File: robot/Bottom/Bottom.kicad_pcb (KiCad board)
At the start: 2 copper layers, 40 x 40 mm, 39 parts, among them M1 Stepper_Motor_bipolar, M2 Stepper_Motor_bipolar, U1 GP2S60, U2 GP2S60, U7 DRV8833PWP, U8 DRV8833PWP

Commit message: Changes to structure
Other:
- outline, holes or cut-outs redrawn
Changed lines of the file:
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@@
-(kicad_pcb (version 20171130) (host pcbnew "(5.1.2)-1")
+(kicad_pcb (version 20171130) (host pcbnew "(5.1.4)-1")
   (general
     (thickness 1.6)
-    (drawings 21)
+    (drawings 23)
     (tracks 283)
     (zones 0)
@@
   )
   (setup
-    (last_trace_width 0.3)
+    (last_trace_width 0.2)
     (user_trace_width 0.2)
     (user_trace_width 0.25)
@@
     )
   )
+  (gr_line (start 159 93) (end 159 110.8) (layer Edge.Cuts) (width 0.1))
+  (gr_line (start 153 110.8) (end 159 110.8) (layer Edge.Cuts) (width 0.1))
+  (gr_line (start 153 113) (end 153 110.8) (layer Edge.Cuts) (width 0.1))
+  (gr_line (start 193 110.8) (end 187 110.8) (layer Edge.Cuts) (width 0.1))
+  (gr_line (start 187 93) (end 187 110.8) (layer Edge.Cuts) (width 0.1))
+  (gr_line (start 193 113) (end 193 110.8) (layer Edge.Cuts) (width 0.1))
   (gr_line (start 187 93) (end 193 93) (layer Edge.Cuts) (width 0.1))
   (gr_line (start 159 93) (end 153 93) (layer Edge.Cuts) (width 0.1))
-  (gr_line (start 159 113) (end 159 93) (layer Edge.Cuts) (width 0.1))
-  (gr_line (start 153 113) (end 159 113) (layer Edge.Cuts) (width 0.1))
-  (gr_line (start 187 113) (end 187 93) (layer Edge.Cuts) (width 0.1))
-  (gr_line (start 193 113) (end 187 113) (layer Edge.Cuts) (width 0.1))
   (gr_line (start 153 93) (end 153 78) (layer Edge.Cuts) (width 0.1))
   (gr_line (start 153 118) (end 153 113) (layer Edge.Cuts) (width 0.1))

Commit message: Small changes, connectors
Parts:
- added H20: GND, Custom:Mounting_Pad_Power, F.Cu at (154.2, 115.5)
- added H21: GND, Custom:Mounting_Pad_Power, F.Cu at (191.8, 115.5)
- added J1: Conn_01x02, Custom:BG300-02-A-L-A, F.Cu at (173.0, 102.6)
- C10, C11, C12, C13, C8, C9: footprint Capacitors_SMD:C_0805 -> Capacitor_SMD:C_0805_2012Metric
- R1, R11, R12, R13, R14, R2, R3, R4: footprint Resistors_SMD:R_0805 -> Resistor_SMD:R_0805_2012Metric
- moved M1 1.50 mm to (164.7, 112.8)
- moved M2 1.50 mm to (181.3, 112.8)
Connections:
- U7 pad 8: (no net) -> Net-(U7-Pad8)
- U8 pad 8: (no net) -> Net-(U8-Pad8)
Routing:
- net Net-(M2-Pad1): track 23.7 -> 25.7 mm
- net Net-(M2-Pad3): track 14.4 -> 12.9 mm
- net Net-(M1-Pad3): track 15.7 -> 17.2 mm
- net Net-(M1-Pad1): track 16.3 -> 14.8 mm
- net Net-(M2-Pad2): track 15.8 -> 14.4 mm
- net Net-(M2-Pad4): track 13.3 -> 12.3 mm
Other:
- outline, holes or cut-outs redrawn

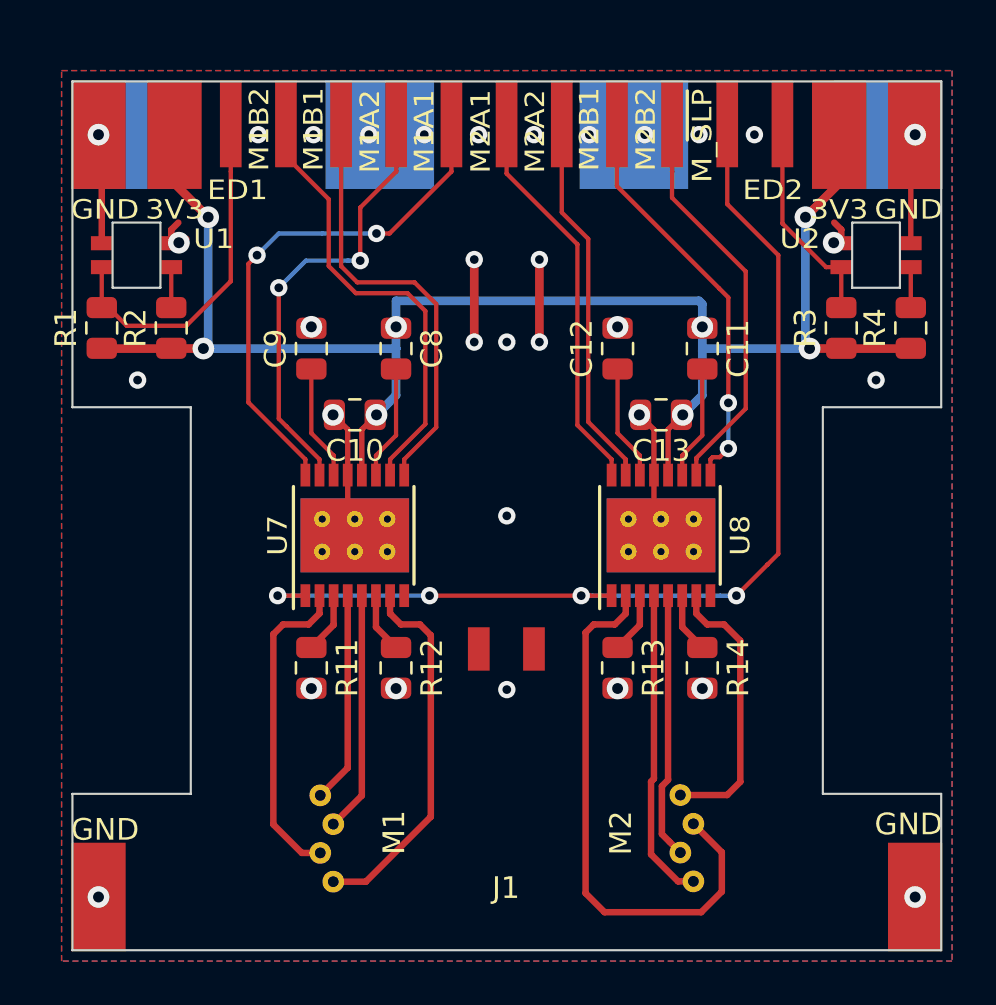
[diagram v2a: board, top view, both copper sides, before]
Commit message: Add VBS, Add Silk deco, small changes
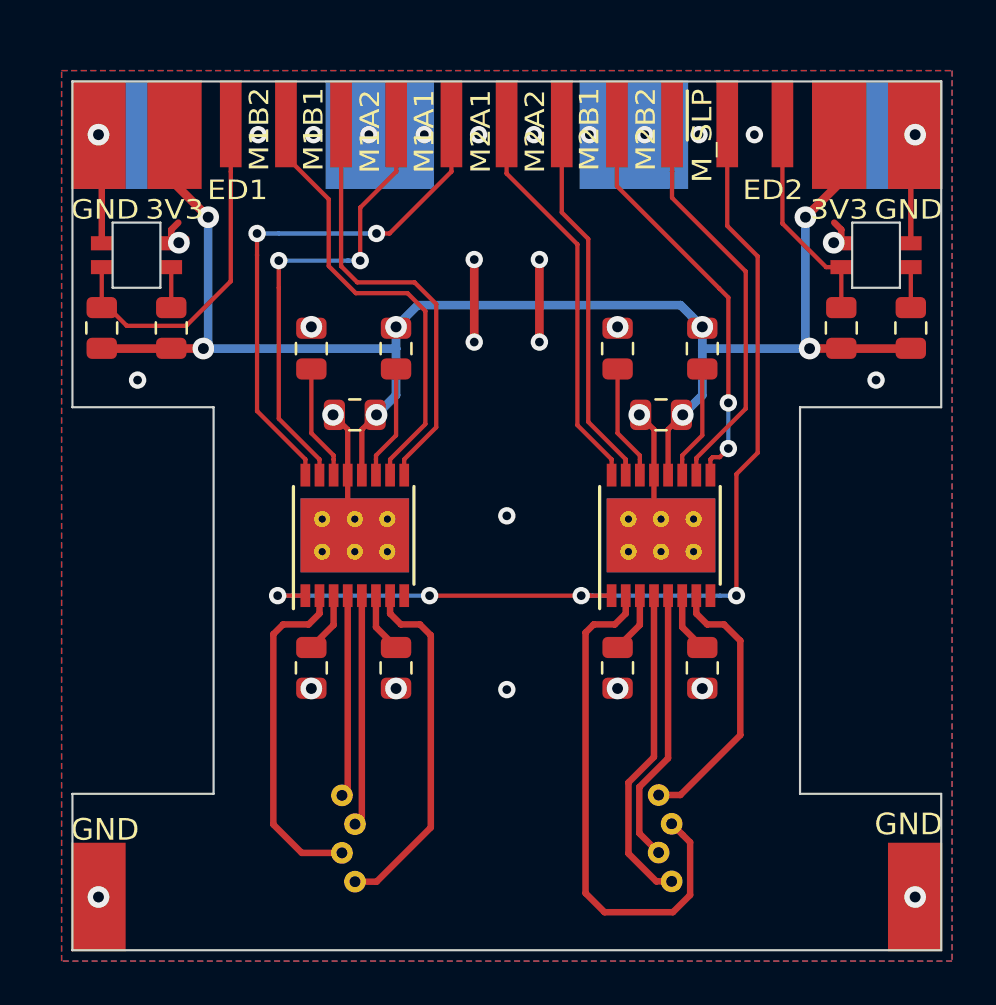
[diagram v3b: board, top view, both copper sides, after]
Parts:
- removed J1: Conn_01x02, Custom:BG300-02-A-L-A
- added G***: LOGO, Print:d2, B.Cu at (173.0, 98.0)
- moved M1 1.00 mm to (165.7, 112.8)
- moved M2 1.00 mm to (180.3, 112.8)
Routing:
- net (no net): track 7.60 -> 0.00 mm, vias 4 -> 0
- net GND: track 24.5 -> 32.1 mm, vias 29 -> 32
- net Net-(M2-Pad1): track 25.7 -> 24.2 mm
- net +3V3: track 78.5 -> 77.0 mm
- net Net-(M1-Pad1): track 14.8 -> 15.8 mm
- net /M1_~SLEEP: track 47.4 -> 46.6 mm
- net /M1_AIN2: track 20.7 -> 21.4 mm
- net Net-(M1-Pad3): track 17.2 -> 16.5 mm
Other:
- outline, holes or cut-outs redrawn

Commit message: Small changes, BOM, Gerbers
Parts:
- H11: value M_~SLP -> M~SLP
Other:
- board text added: "Cuby V0.1"

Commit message: BOM items
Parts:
- C10, C13: value 10µ -> 22µ
- R11, R12, R13, R14: value 0.8 -> 1
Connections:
- U7 pad 8: Net-(U7-Pad8) -> (no net)
- U8 pad 8: Net-(U8-Pad8) -> (no net)
